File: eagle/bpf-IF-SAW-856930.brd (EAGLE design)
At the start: 18 x 16 mm, 3 parts, among them J1 142-0701-851, J2 142-0701-851, U1 Qorvo 856930

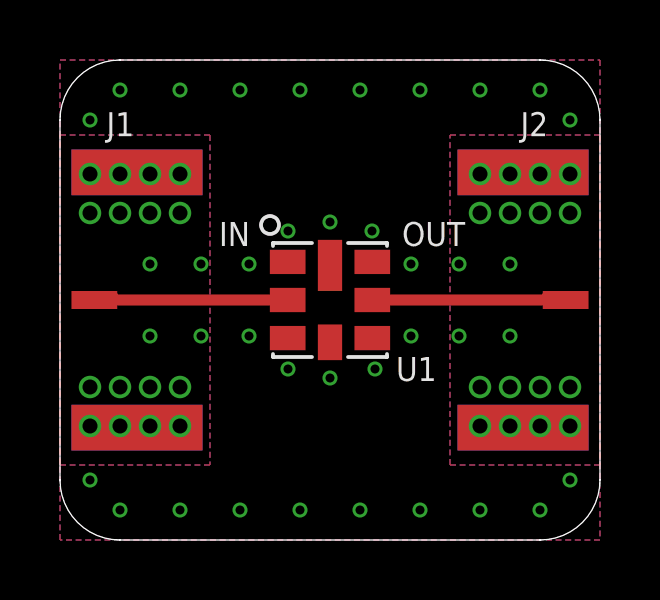
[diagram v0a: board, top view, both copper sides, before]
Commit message: Update SMA footprint
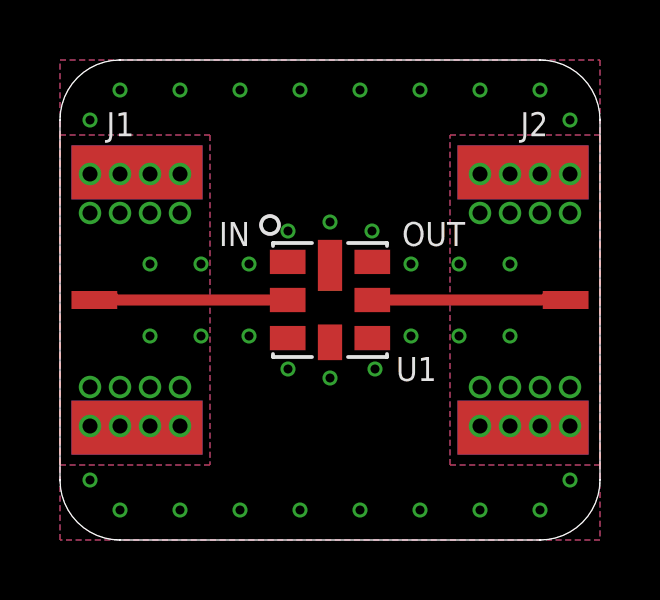
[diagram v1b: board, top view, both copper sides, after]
